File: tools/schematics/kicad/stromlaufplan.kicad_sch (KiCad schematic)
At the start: 4 parts, among them K1 Relaismodul (6 Kanaele), U1 MCP23017, U2 I2C Level-Shifter (4-Kanal, b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

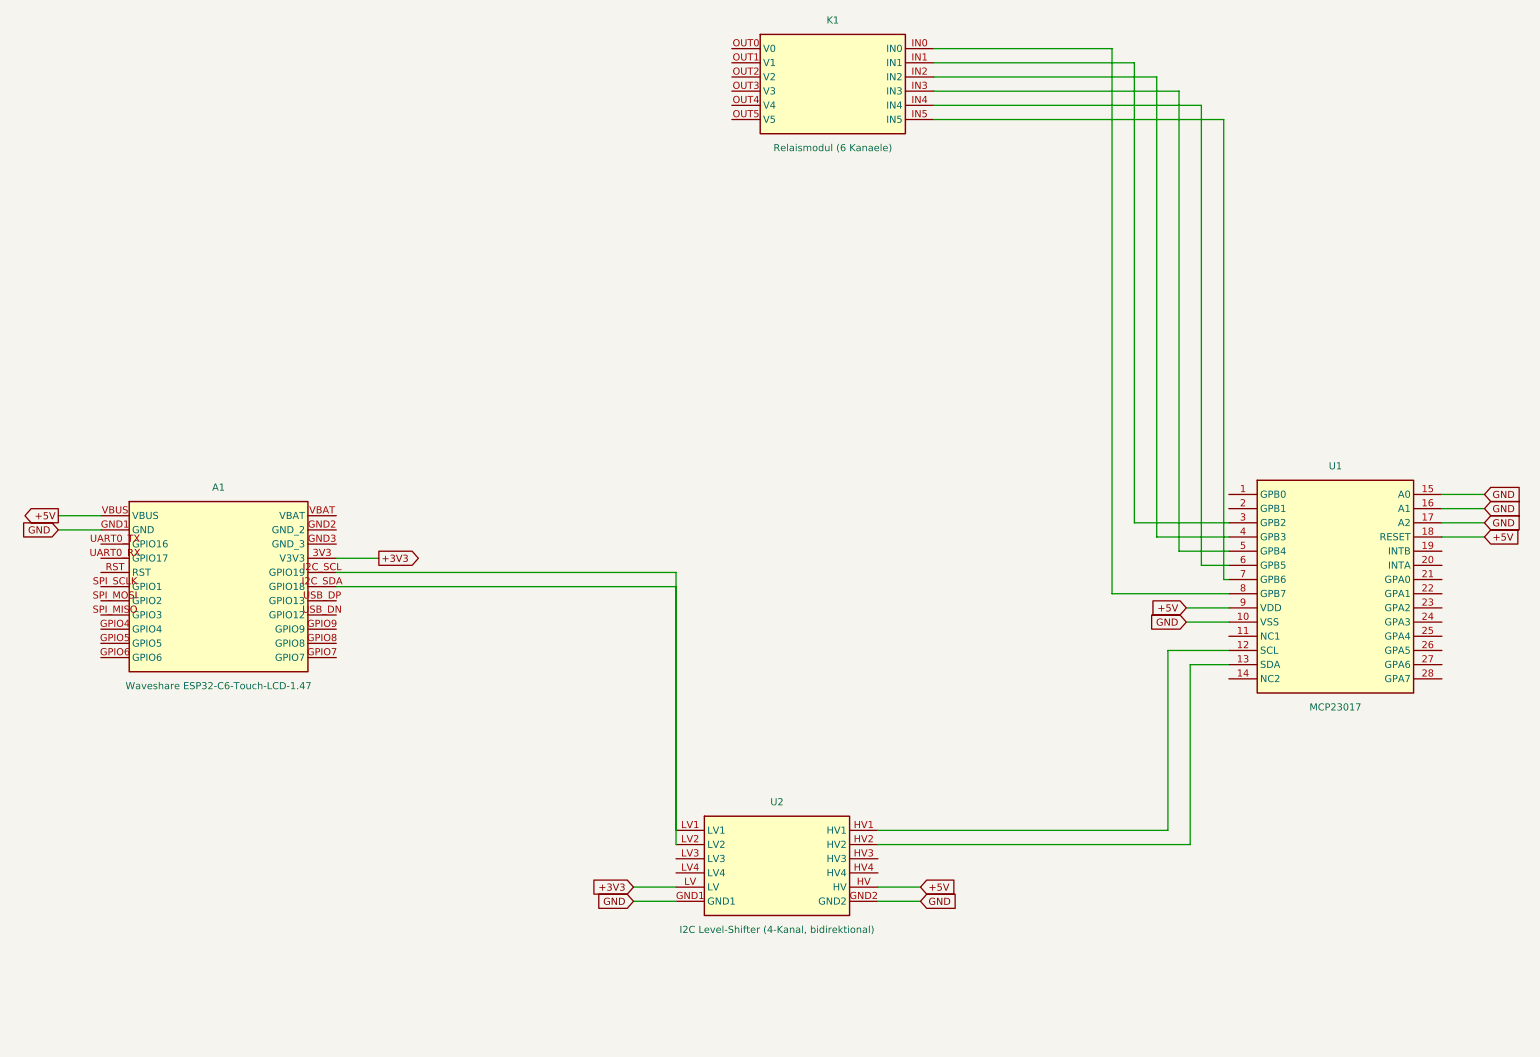
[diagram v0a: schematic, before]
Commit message: Schematics: KiCad-Symbole auf Standard-DIP-Pinbelegung korrigiert
Rechte Pinreihe wickelt jetzt wie beim echten IC-Gehaeuse um (Pin 1
oben links -> runter -> rechts wieder hoch), statt einfach von oben
nach unten durchnummeriert zu sein. Beim MCP23017 stimmt das jetzt mit
dem Microchip-Datenblatt-Pinout ueberein (Pin 15=A0 unten, Pin 28=GPA7
oben). Ausserdem: semantische elektrische Pin-Typen (power_in/input/
output/no_connect statt pauschal bidirektional) und Pin-1-Markierungspunkt.

Co-Authored-By: Claude Sonnet 5 <noreply@anthropic.com>
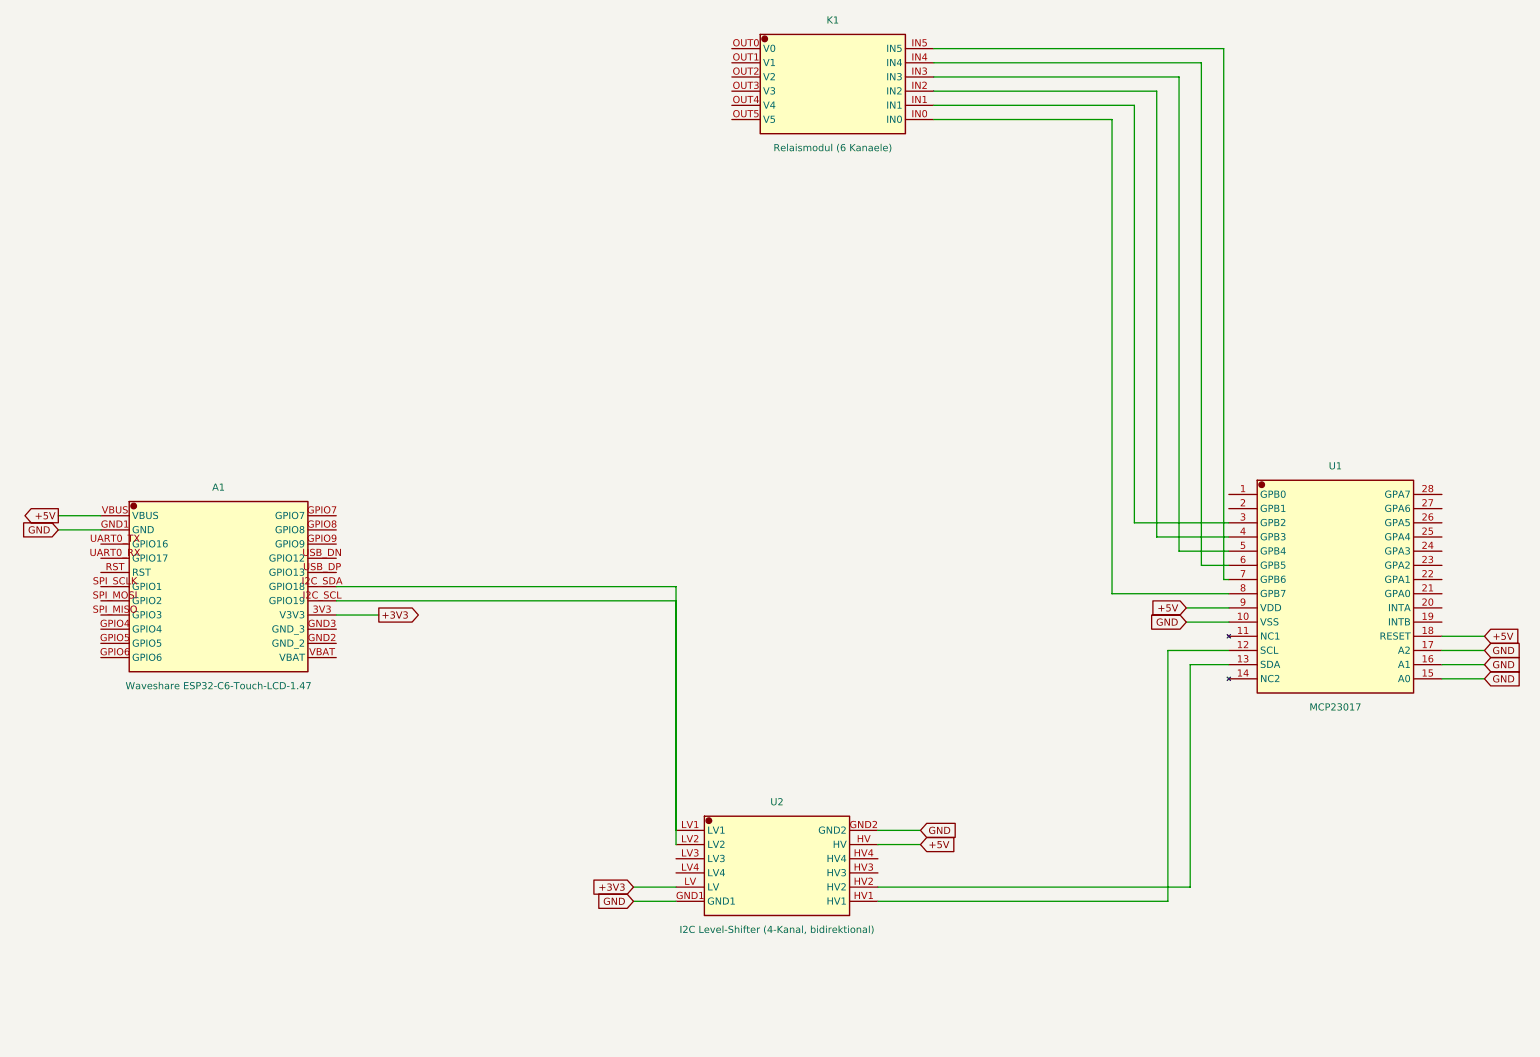
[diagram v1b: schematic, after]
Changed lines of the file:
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@@
 		(pin "GPIO5")
 		(pin "GPIO6")
+		(pin "GPIO7")
+		(pin "GPIO8")
+		(pin "GPIO9")
+		(pin "USB_DN")
+		(pin "USB_DP")
+		(pin "I2C_SDA")
+		(pin "I2C_SCL")
+		(pin "3V3")
+		(pin "GND3")
+		(pin "GND2")
 		(pin "VBAT")
-		(pin "GND2")
-		(pin "GND3")
-		(pin "3V3")
-		(pin "I2C_SCL")
-		(pin "I2C_SDA")
-		(pin "USB_DP")
-		(pin "USB_DN")
-		(pin "GPIO9")
-		(pin "GPIO8")
-		(pin "GPIO7")
 	)
 	(symbol
@@
 		(pin "13")
 		(pin "14")
+		(pin "28")
+		(pin "27")
+		(pin "26")
+		(pin "25")
+		(pin "24")
+		(pin "23")
+		(pin "22")
+		(pin "21")
+		(pin "20")
+		(pin "19")
+		(pin "18")
+		(pin "17")
+		(pin "16")
 		(pin "15")
-		(pin "16")
-		(pin "17")
-		(pin "18")
-		(pin "19")
-		(pin "20")
-		(pin "21")
-		(pin "22")
-		(pin "23")
-		(pin "24")
-		(pin "25")
-		(pin "26")
-		(pin "27")
-		(pin "28")
 	)
 	(symbol
@@
 		(pin "OUT4")
 		(pin "OUT5")
+		(pin "IN5")
+		(pin "IN4")
+		(pin "IN3")
+		(pin "IN2")
+		(pin "IN1")
 		(pin "IN0")
-		(pin "IN1")
-		(pin "IN2")
-		(pin "IN3")
-		(pin "IN4")
-		(pin "IN5")
 	)
 	(symbol
@@
 		(pin "LV")
 		(pin "GND1")
+		(pin "GND2")
+		(pin "HV")
+		(pin "HV4")
+		(pin "HV3")
+		(pin "HV2")
 		(pin "HV1")
-		(pin "HV2")
-		(pin "HV3")
-		(pin "HV4")
-		(pin "HV")
-		(pin "GND2")
 	)
-	(wire (pts (xy 81.08 147.46) (xy 141.92 147.46)) (stroke (width 0.1524) (type default)))
-	(wire (pts (xy 141.92 147.46) (xy 141.92 193.65)) (stroke (width 0.1524) (type default)))
+	(wire (pts (xy 81.08 152.54) (xy 141.92 152.54)) (stroke (width 0.1524) (type default)))
+	(wire (pts (xy 141.92 152.54) (xy 141.92 193.65)) (stroke (width 0.1524) (type default)))
 	(wire (pts (xy 81.08 150.00) (xy 141.92 150.00)) (stroke (width 0.1524) (type default)))
 	(wire (pts (xy 141.92 150.00) (xy 141.92 196.19)) (stroke (width 0.1524) (type default)))
-	(wire (pts (xy 178.08 193.65) (xy 230.00 193.65)) (stroke (width 0.1524) (type default)))
-	(wire (pts (xy 230.00 193.65) (xy 230.00 161.43)) (stroke (width 0.1524) (type default)))
+	(wire (pts (xy 178.08 206.35) (xy 230.00 206.35)) (stroke (width 0.1524) (type default)))
+	(wire (pts (xy 230.00 206.35) (xy 230.00 161.43)) (stroke (width 0.1524) (type default)))
 	(wire (pts (xy 230.00 161.43) (xy 240.92 161.43)) (stroke (width 0.1524) (type default)))
-	(wire (pts (xy 178.08 196.19) (xy 234.00 196.19)) (stroke (width 0.1524) (type default)))
-	(wire (pts (xy 234.00 196.19) (xy 234.00 163.97)) (stroke (width 0.1524) (type default)))
+	(wire (pts (xy 178.08 203.81) (xy 234.00 203.81)) (stroke (width 0.1524) (type default)))
+	(wire (pts (xy 234.00 203.81) (xy 234.00 163.97)) (stroke (width 0.1524) (type default)))
 	(wire (pts (xy 234.00 163.97) (xy 240.92 163.97)) (stroke (width 0.1524) (type default)))
 	(wire (pts (xy 240.92 151.27) (xy 220.00 151.27)) (stroke (width 0.1524) (type default)))
-	(wire (pts (xy 220.00 151.27) (xy 220.00 53.65)) (stroke (width 0.1524) (type default)))
-	(wire (pts (xy 220.00 53.65) (xy 188.08 53.65)) (stroke (width 0.1524) (type default)))
+	(wire (pts (xy 220.00 151.27) (xy 220.00 66.35)) (stroke (width 0.1524) (type default)))
+	(wire (pts (xy 220.00 66.35) (xy 188.08 66.35)) (stroke (width 0.1524) (type default)))
 	(wire (pts (xy 240.92 138.57) (xy 224.00 138.57)) (stroke (width 0.1524) (type default)))
-	(wire (pts (xy 224.00 138.57) (xy 224.00 56.19)) (stroke (width 0.1524) (type default)))
-	(wire (pts (xy 224.00 56.19) (xy 188.08 56.19)) (stroke (width 0.1524) (type default)))
+	(wire (pts (xy 224.00 138.57) (xy 224.00 63.81)) (stroke (width 0.1524) (type default)))
+	(wire (pts (xy 224.00 63.81) (xy 188.08 63.81)) (stroke (width 0.1524) (type default)))
 	(wire (pts (xy 240.92 141.11) (xy 228.00 141.11)) (stroke (width 0.1524) (type default)))
-	(wire (pts (xy 228.00 141.11) (xy 228.00 58.73)) (stroke (width 0.1524) (type default)))
-	(wire (pts (xy 228.00 58.73) (xy 188.08 58.73)) (stroke (width 0.1524) (type default)))
+	(wire (pts (xy 228.00 141.11) (xy 228.00 61.27)) (stroke (width 0.1524) (type default)))
+	(wire (pts (xy 228.00 61.27) (xy 188.08 61.27)) (stroke (width 0.1524) (type default)))
 	(wire (pts (xy 240.92 143.65) (xy 232.00 143.65)) (stroke (width 0.1524) (type default)))
-	(wire (pts (xy 232.00 143.65) (xy 232.00 61.27)) (stroke (width 0.1524) (type default)))
-	(wire (pts (xy 232.00 61.27) (xy 188.08 61.27)) (stroke (width 0.1524) (type default)))
+	(wire (pts (xy 232.00 143.65) (xy 232.00 58.73)) (stroke (width 0.1524) (type default)))
+	(wire (pts (xy 232.00 58.73) (xy 188.08 58.73)) (stroke (width 0.1524) (type default)))
 	(wire (pts (xy 240.92 146.19) (xy 236.00 146.19)) (stroke (width 0.1524) (type default)))
-	(wire (pts (xy 236.00 146.19) (xy 236.00 63.81)) (stroke (width 0.1524) (type default)))
-	(wire (pts (xy 236.00 63.81) (xy 188.08 63.81)) (stroke (width 0.1524) (type default)))
+	(wire (pts (xy 236.00 146.19) (xy 236.00 56.19)) (stroke (width 0.1524) (type default)))
+	(wire (pts (xy 236.00 56.19) (xy 188.08 56.19)) (stroke (width 0.1524) (type default)))
 	(wire (pts (xy 240.92 148.73) (xy 240.00 148.73)) (stroke (width 0.1524) (type default)))
-	(wire (pts (xy 240.00 148.73) (xy 240.00 66.35)) (stroke (width 0.1524) (type default)))
-	(wire (pts (xy 240.00 66.35) (xy 188.08 66.35)) (stroke (width 0.1524) (type default)))
+	(wire (pts (xy 240.00 148.73) (xy 240.00 53.65)) (stroke (width 0.1524) (type default)))
+	(wire (pts (xy 240.00 53.65) (xy 188.08 53.65)) (stroke (width 0.1524) (type default)))
 	(wire (pts (xy 38.92 137.30) (xy 31.30 137.30)) (stroke (width 0.1524) (type default)))
 	(global_label "+5V" (shape output) (at 31.30 137.30 180)
 		(effects (font (size 1.27 1.27)) (justify right))
 	)
-	(wire (pts (xy 81.08 144.92) (xy 88.70 144.92)) (stroke (width 0.1524) (type default)))
-	(global_label "+3V3" (shape output) (at 88.70 144.92 0)
+	(wire (pts (xy 81.08 155.08) (xy 88.70 155.08)) (stroke (width 0.1524) (type default)))
+	(global_label "+3V3" (shape output) (at 88.70 155.08 0)
 		(effects (font (size 1.27 1.27)) (justify left))
 	)
@@
 		(effects (font (size 1.27 1.27)) (justify right))
 	)
-	(wire (pts (xy 178.08 203.81) (xy 185.70 203.81)) (stroke (width 0.1524) (type default)))
-	(global_label "+5V" (shape input) (at 185.70 203.81 0)
+	(wire (pts (xy 178.08 196.19) (xy 185.70 196.19)) (stroke (width 0.1524) (type default)))
+	(global_label "+5V" (shape input) (at 185.70 196.19 0)
 		(effects (font (size 1.27 1.27)) (justify left))
 	)
-	(wire (pts (xy 178.08 206.35) (xy 185.70 206.35)) (stroke (width 0.1524) (type default)))
-	(global_label "GND" (shape input) (at 185.70 206.35 0)
+	(wire (pts (xy 178.08 193.65) (xy 185.70 193.65)) (stroke (width 0.1524) (type default)))
+	(global_label "GND" (shape input) (at 185.70 193.65 0)
 		(effects (font (size 1.27 1.27)) (justify left))
 	)
@@
 		(effects (font (size 1.27 1.27)) (justify right))
 	)
-	(wire (pts (xy 279.08 141.11) (xy 286.70 141.11)) (stroke (width 0.1524) (type default)))
-	(global_label "+5V" (shape input) (at 286.70 141.11 0)
+	(wire (pts (xy 279.08 158.89) (xy 286.70 158.89)) (stroke (width 0.1524) (type default)))
+	(global_label "+5V" (shape input) (at 286.70 158.89 0)
 		(effects (font (size 1.27 1.27)) (justify left))
 	)
-	(wire (pts (xy 279.08 133.49) (xy 286.70 133.49)) (stroke (width 0.1524) (type default)))
-	(global_label "GND" (shape input) (at 286.70 133.49 0)
+	(wire (pts (xy 279.08 166.51) (xy 286.70 166.51)) (stroke (width 0.1524) (type default)))
+	(global_label "GND" (shape input) (at 286.70 166.51 0)
 		(effects (font (size 1.27 1.27)) (justify left))
 	)
-	(wire (pts (xy 279.08 136.03) (xy 286.70 136.03)) (stroke (width 0.1524) (type default)))
-	(global_label "GND" (shape input) (at 286.70 136.03 0)
+	(wire (pts (xy 279.08 163.97) (xy 286.70 163.97)) (stroke (width 0.1524) (type default)))
+	(global_label "GND" (shape input) (at 286.70 163.97 0)
 		(effects (font (size 1.27 1.27)) (justify left))
 	)
-	(wire (pts (xy 279.08 138.57) (xy 286.70 138.57)) (stroke (width 0.1524) (type default)))
-	(global_label "GND" (shape input) (at 286.70 138.57 0)
+	(wire (pts (xy 279.08 161.43) (xy 286.70 161.43)) (stroke (width 0.1524) (type default)))
+	(global_label "GND" (shape input) (at 286.70 161.43 0)
 		(effects (font (size 1.27 1.27)) (justify left))
 	)
